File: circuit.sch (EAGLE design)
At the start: 8 parts

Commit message: merged display code into main code, added sch
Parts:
- added IC1: 74HC595N, 74xx-eu:74HC595N
- added R2, R3: 330, HyTechDevices:RESISTORPTH-1/4W
- added R4: 1k, HyTechDevices:RESISTORPTH-1/4W
- added S2: (no value), switch-omron:40-XX
- added U$6: DUAL_7SEG_DISPLAY, HyTechDevices:DUAL_7SEG_DISPLAY
- added U$7, U$8: 2N9304, HyTechDevices:2N9304
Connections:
- new net BJT1_CTRL: R2.1, U$7.BASE
- new net BJT2_CTRL: R3.1, U$8.BASE
- new net D28: R2.2, U$1.D28
- new net D29: R3.2, U$1.D29
- new net DIG1_COL: U$6.P$16, U$7.COLLECTOR
- new net DIG2_COL: U$6.P$11, U$8.COLLECTOR
- new net N$1: IC1A.QE, U$6.P$1
- new net N$10: IC1A.QG, U$6.P$13
- new net N$11: IC1A.QH, U$6.P$6
- new net N$12: R4.1, S2.P, U$1.A15
- new net N$3: IC1A.QB, U$6.P$10
- new net N$4: IC1A.QC, U$6.P$9
- new net N$7: IC1A.QD, U$6.P$7
- new net N$8: IC1A.QA, U$6.P$12
- new net N$9: IC1A.QF, U$6.P$18
- new net RCLK: IC1A.RCK, U$1.A19
- new net SER: IC1A.SER, U$1.A17
- new net SRCLK: IC1A.SCK, U$1.A18
- new net SRCLR: IC1A.SCL, U$1.A20
- net +3V3: now also IC1P.VCC, S2.S
- net GND: now also IC1A.G, IC1P.GND, R4.2, U$7.EMITTER, U$8.EMITTER
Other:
- note added: ""unfreeze" button"
- note added: "BMMCC orientation logger - made by Soohyun Kim"
- note added: "adafruit sensor"
- note added: "record button"
- moved on the sheet: R1, S1

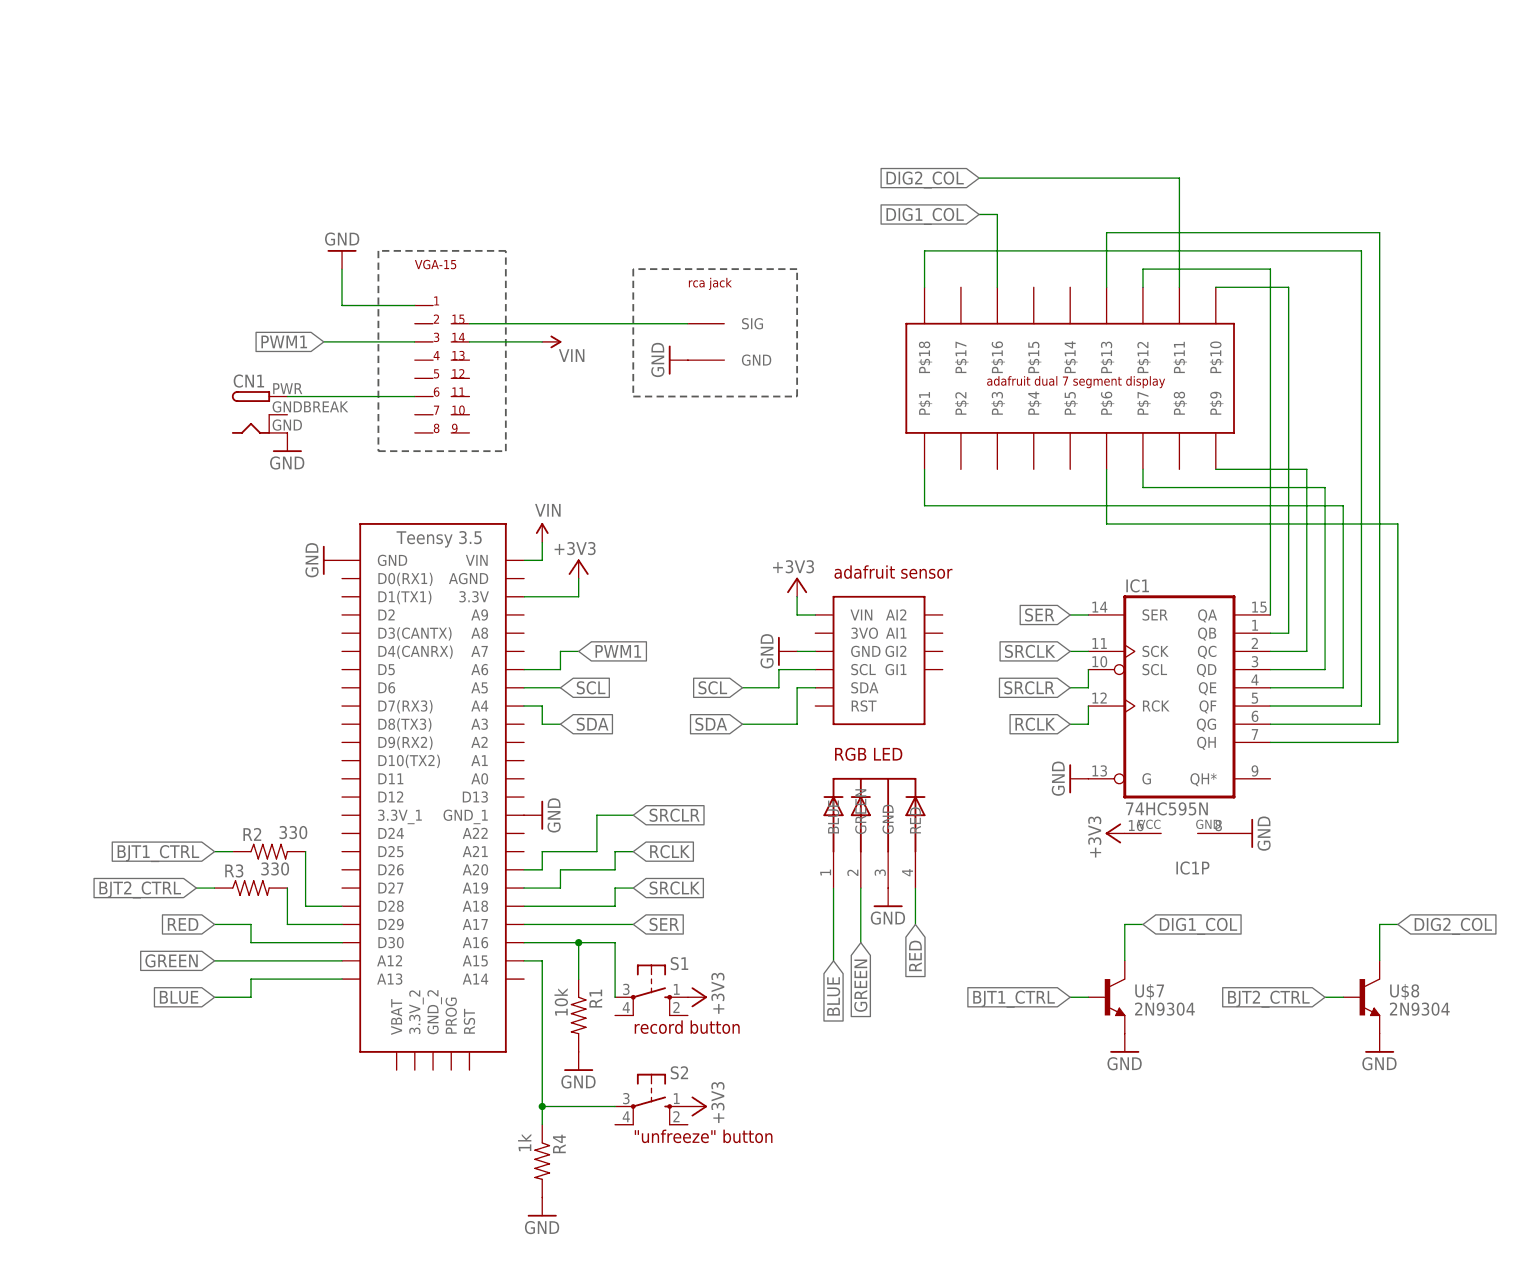
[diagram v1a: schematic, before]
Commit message: added board for main pcb
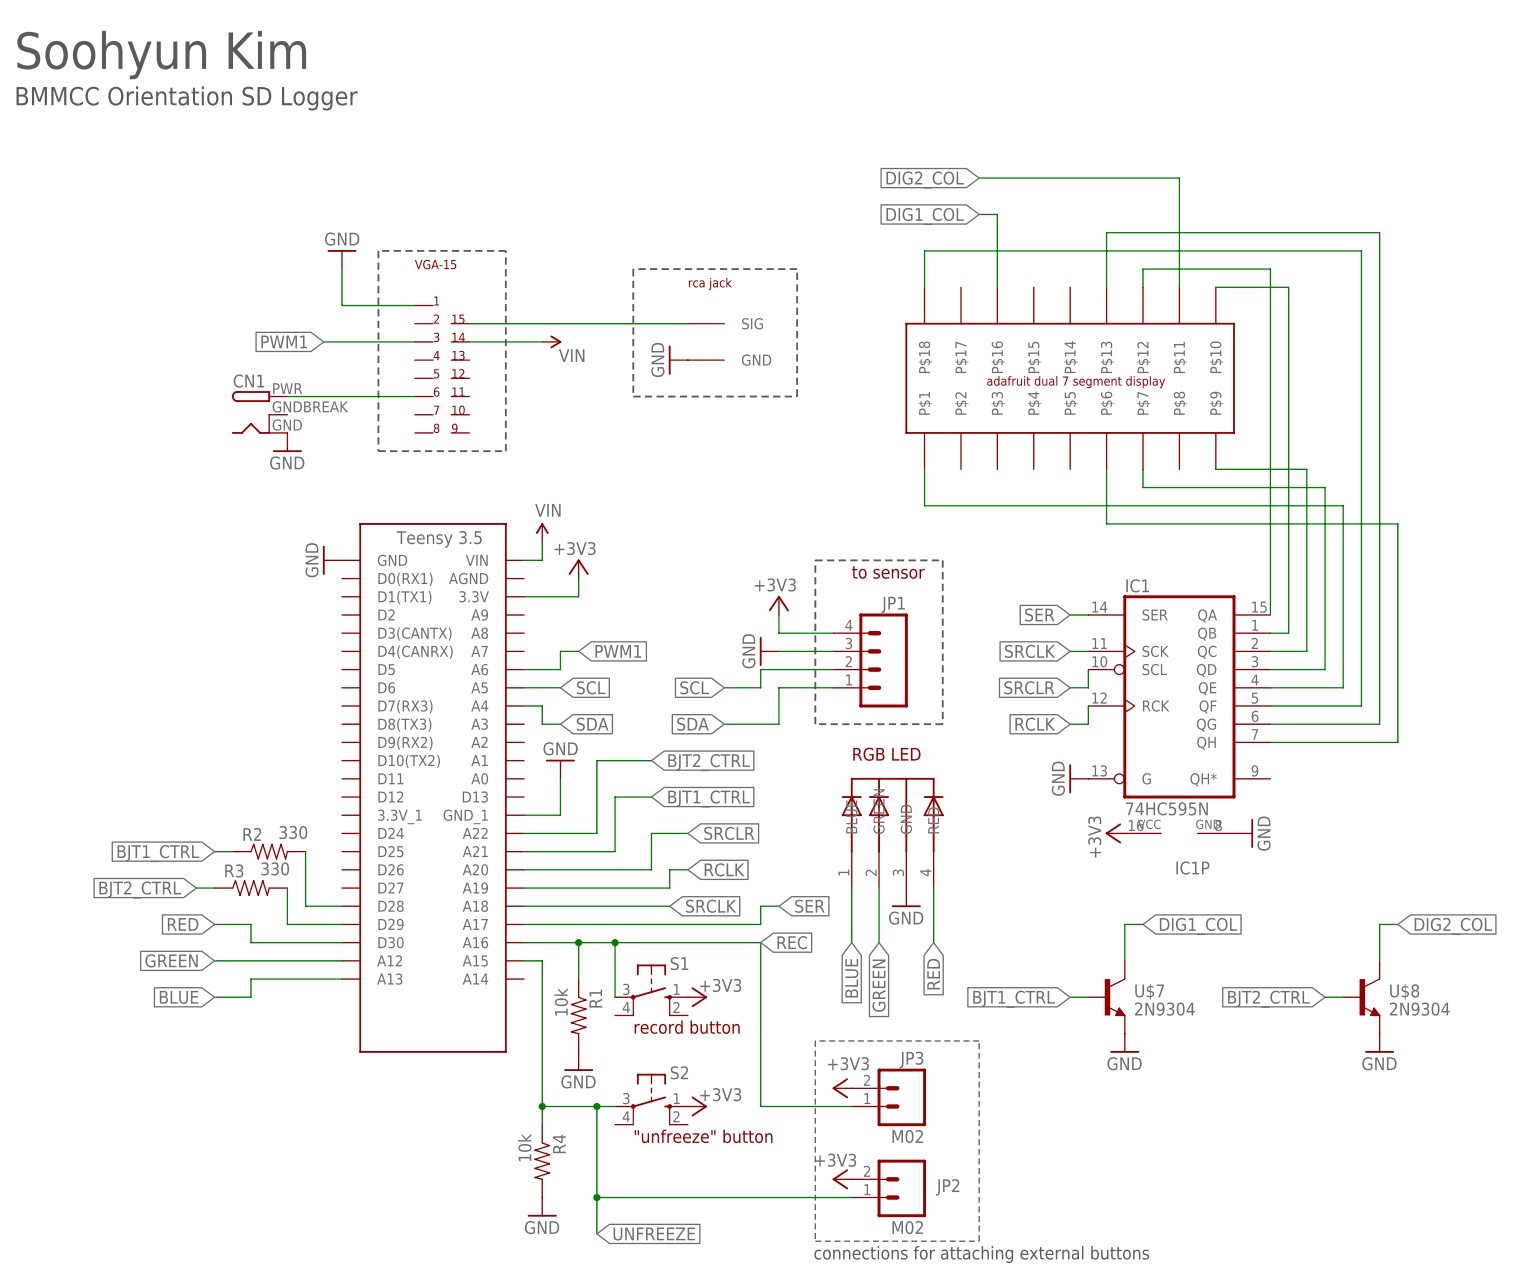
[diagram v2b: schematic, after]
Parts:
- removed U$5: RCA, HyTechDevices:RCA
- added JP1: (no value), HyTechDevices:M04
- added JP2, JP3: M02, HyTechDevices:M02
- R4: value 1k -> 10k
- U$1: value TEENSY_3.5_EXT -> TEENSY_3.5; device HyTechDevices:TEENSY_3.5_EXT -> HyTechDevices:TEENSY_3.5
- U$3: value ADAFRUIT_9DOF -> RCA; device HyTechDevices:ADAFRUIT_9DOF -> HyTechDevices:RCA
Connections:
- removed net N$12: R4.1, S2.P, U$1.A15
- removed net N$2: R1.1, S1.P, U$1.A16
- new net REC: JP3.1, R1.1, S1.P, U$1.A16
- new net UNFREEZE: JP2.1, R4.1, S2.P, U$1.A15
- net +3V3: now also JP1.4, JP2.2, JP3.2; no longer U$3.VIN
- net BJT1_CTRL: now also U$1.A21
- net BJT2_CTRL: now also U$1.A22
- net GND: now also JP1.3; no longer U$5.GND
- net N$5: now also U$3.SIG; no longer U$5.SIG
- net SCL: now also JP1.2; no longer U$3.SCL
- net SDA: now also JP1.1; no longer U$3.SDA
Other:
- note added: "BMMCC Orientation SD Logger"
- note added: "Soohyun Kim"
- note added: "connections for attaching external buttons"
- note added: "to sensor"
- note removed: "BMMCC orientation logger - made by Soohyun Kim"
- note removed: "adafruit sensor"

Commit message: final?
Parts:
- added U$5: SLIDE_SWITCH, HyTechDevices:SLIDE_SWITCH
- U$4: value LED_5MM_RGB -> LED_5MM_RGBSTRAIGHT; device HyTechDevices:LED_5MM_RGB -> HyTechDevices:LED_5MM_RGBSTRAIGHT
- renumbered S1 to S3, S2 to S4
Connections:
- new net N$2: U$2.P$14, U$5.P
- net VIN: now also U$5.S; no longer U$2.P$14
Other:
- note added: "power switch / reset"
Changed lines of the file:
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@@
 <part name="GND5" library="HyTechSymbols" deviceset="GND" device=""/>
 <part name="GND6" library="HyTechSymbols" deviceset="GND" device=""/>
-<part name="S1" library="switch-omron" library_urn="urn:adsk.eagle:library:377" deviceset="40-XX" device="" package3d_urn="urn:adsk.eagle:package:27483/1"/>
 <part name="+3V3" library="supply1" library_urn="urn:adsk.eagle:library:371" deviceset="+3V3" device=""/>
-<part name="U$4" library="HyTechDevices" deviceset="LED_5MM_RGB" device=""/>
 <part name="GND7" library="HyTechSymbols" deviceset="GND" device=""/>
 <part name="GND8" library="HyTechSymbols" deviceset="GND" device=""/>
@@
 <part name="R2" library="HyTechDevices" deviceset="RESISTOR" device="PTH-1/4W" value="330"/>
 <part name="R3" library="HyTechDevices" deviceset="RESISTOR" device="PTH-1/4W" value="330"/>
-<part name="S2" library="switch-omron" library_urn="urn:adsk.eagle:library:377" deviceset="40-XX" device="" package3d_urn="urn:adsk.eagle:package:27483/1"/>
 <part name="+3V5" library="supply1" library_urn="urn:adsk.eagle:library:371" deviceset="+3V3" device=""/>
 <part name="R4" library="HyTechDevices" deviceset="RESISTOR" device="PTH-1/4W" value="10k"/>
@@
 <part name="U$1" library="HyTechDevices" deviceset="TEENSY_3.5" device=""/>
 <part name="U$2" library="HyTechDevices" deviceset="VGA-15" device=""/>
+<part name="U$4" library="HyTechDevices" deviceset="LED_5MM_RGB" device="STRAIGHT"/>
+<part name="U$5" library="HyTechDevices" deviceset="SLIDE_SWITCH" device=""/>
+<part name="S3" library="switch-omron" deviceset="40-XX" device="" package3d_urn="urn:adsk.eagle:package:27483/1"/>
+<part name="S4" library="switch-omron" deviceset="40-XX" device="" package3d_urn="urn:adsk.eagle:package:27483/1"/>
 </parts>
 <sheets>
@@
 <wire x1="106.68" y1="-3.556" x2="106.68" y2="24.384" width="0.1524" layer="97" style="shortdash"/>
 <wire x1="106.68" y1="24.384" x2="83.82" y2="24.384" width="0.1524" layer="97" style="shortdash"/>
+<text x="58.42" y="106.68" size="1.778" layer="94">power switch / reset</text>
 </plain>
 <instances>
@@
 <attribute name="VALUE" x="7.62" y="104.14" size="1.778" layer="96"/>
 </instance>
-<instance part="SUPPLY1" gate="G$1" x="45.72" y="121.92" smashed="yes" rot="R270">
-<attribute name="VALUE" x="51.816" y="120.904" size="1.778" layer="96" rot="R180"/>
+<instance part="SUPPLY1" gate="G$1" x="55.88" y="104.14" smashed="yes" rot="R270">
+<attribute name="VALUE" x="61.976" y="103.124" size="1.778" layer="96" rot="R180"/>
 </instance>
 <instance part="SUPPLY2" gate="G$1" x="45.72" y="93.98" smashed="yes">
@@
 <attribute name="VALUE" x="12.7" y="93.98" size="1.778" layer="96" rot="R270"/>
 </instance>
-<instance part="S1" gate="1" x="60.96" y="30.48" smashed="yes" rot="R270">
-<attribute name="NAME" x="63.5" y="34.29" size="1.778" layer="95"/>
-<attribute name="VALUE" x="64.135" y="34.29" size="1.778" layer="96"/>
-</instance>
 <instance part="+3V3" gate="G$1" x="68.58" y="30.48" smashed="yes" rot="R270">
 <attribute name="VALUE" x="73.66" y="33.02" size="1.778" layer="96" rot="R180"/>
 </instance>
-<instance part="U$4" gate="G$1" x="96.52" y="60.96" smashed="yes"/>
 <instance part="GND7" gate="1" x="96.52" y="43.18" smashed="yes">
 <attribute name="VALUE" x="93.98" y="40.64" size="1.778" layer="96"/>
@@
 <attribute name="VALUE" x="6.35" y="47.498" size="1.778" layer="96"/>
 </instance>
-<instance part="S2" gate="1" x="60.96" y="15.24" smashed="yes" rot="R270">
-<attribute name="NAME" x="63.5" y="19.05" size="1.778" layer="95"/>
-<attribute name="VALUE" x="64.135" y="19.05" size="1.778" layer="96"/>
-</instance>
 <instance part="+3V5" gate="G$1" x="68.58" y="15.24" smashed="yes" rot="R270">
 <attribute name="VALUE" x="73.66" y="17.78" size="1.778" layer="96" rot="R180"/>
@@
 <instance part="U$1" gate="G$1" x="20.32" y="22.86" smashed="yes"/>
 <instance part="U$2" gate="G$1" x="27.94" y="127" smashed="yes"/>
+<instance part="U$4" gate="G$1" x="96.52" y="60.96" smashed="yes"/>
+<instance part="U$5" gate="G$1" x="50.8" y="109.22" smashed="yes" rot="R270"/>
+<instance part="S3" gate="1" x="60.96" y="30.48" smashed="yes" rot="R270">
+<attribute name="VALUE" x="64.135" y="34.29" size="1.778" layer="96"/>
+</instance>
+<instance part="S4" gate="1" x="60.96" y="15.24" smashed="yes" rot="R270">
+<attribute name="VALUE" x="64.135" y="19.05" size="1.778" layer="96"/>
+</instance>
 </instances>
 <busses>
@@
 </segment>
 <segment>
-<pinref part="U$4" gate="G$1" pin="GND"/>
-<pinref part="GND7" gate="1" pin="GND"/>
-</segment>
-<segment>
 <pinref part="IC1" gate="P" pin="GND"/>
 <pinref part="GND9" gate="1" pin="GND"/>
@@
 <pinref part="U$1" gate="G$1" pin="GND"/>
 </segment>
+<segment>
+<pinref part="GND7" gate="1" pin="GND"/>
+<pinref part="U$4" gate="G$1" pin="GND"/>
+</segment>
 </net>
 <net name="VIN" class="0">
@@
 </segment>
 <segment>
-<wire x1="45.72" y1="121.92" x2="35.56" y2="121.92" width="0.1524" layer="91"/>
+<pinref part="U$5" gate="G$1" pin="S"/>
 <pinref part="SUPPLY1" gate="G$1" pin="VIN"/>
-<pinref part="U$2" gate="G$1" pin="P$14"/>
 </segment>
 </net>
@@
 </segment>
 <segment>
-<pinref part="S1" gate="1" pin="S"/>
-<pinref part="+3V3" gate="G$1" pin="+3V3"/>
-</segment>
-<segment>
 <pinref part="IC1" gate="P" pin="VCC"/>
 <pinref part="+3V4" gate="G$1" pin="+3V3"/>
 </segment>
 <segment>
-<pinref part="S2" gate="1" pin="S"/>
-<pinref part="+3V5" gate="G$1" pin="+3V3"/>
-</segment>
-<segment>
 <pinref part="JP2" gate="G$1" pin="2"/>
 <pinref part="+3V6" gate="G$1" pin="+3V3"/>
@@
 <pinref part="JP3" gate="G$1" pin="2"/>
 <pinref part="+3V7" gate="G$1" pin="+3V3"/>
+</segment>
+<segment>
+<pinref part="+3V3" gate="G$1" pin="+3V3"/>
+<pinref part="S3" gate="1" pin="S"/>
+</segment>
+<segment>
+<pinref part="+3V5" gate="G$1" pin="+3V3"/>
+<pinref part="S4" gate="1" pin="S"/>
 </segment>
 </net>
@@
 <net name="RED" class="0">
 <segment>
-<pinref part="U$4" gate="G$1" pin="RED"/>
 <wire x1="100.33" y1="45.72" x2="100.33" y2="38.1" width="0.1524" layer="91"/>
 <label x="100.33" y="38.1" size="1.778" layer="95" rot="R270" xref="yes"/>
+<pinref part="U$4" gate="G$1" pin="RED"/>
 </segment>
 <segment>
@@
 <net name="GREEN" class="0">
 <segment>
-<pinref part="U$4" gate="G$1" pin="GREEN"/>
 <wire x1="92.71" y1="45.72" x2="92.71" y2="38.1" width="0.1524" layer="91"/>
 <label x="92.71" y="38.1" size="1.778" layer="95" rot="R270" xref="yes"/>
+<pinref part="U$4" gate="G$1" pin="GREEN"/>
 </segment>
 <segment>
@@
 <net name="BLUE" class="0">
 <segment>
-<pinref part="U$4" gate="G$1" pin="BLUE"/>
 <wire x1="88.9" y1="45.72" x2="88.9" y2="38.1" width="0.1524" layer="91"/>
 <label x="88.9" y="38.1" size="1.778" layer="95" rot="R270" xref="yes"/>
+<pinref part="U$4" gate="G$1" pin="BLUE"/>
 </segment>
 <segment>
@@
 <net name="REC" class="0">
 <segment>
-<pinref part="S1" gate="1" pin="P"/>
 <wire x1="55.88" y1="38.1" x2="55.88" y2="30.48" width="0.1524" layer="91"/>
 <wire x1="43.18" y1="38.1" x2="50.8" y2="38.1" width="0.1524" layer="91"/>
@@
 <label x="76.2" y="38.1" size="1.778" layer="95" xref="yes"/>
 <pinref part="U$1" gate="G$1" pin="A16"/>
+<pinref part="S3" gate="1" pin="P"/>
 </segment>
 </net>
@@
 <wire x1="45.72" y1="35.56" x2="45.72" y2="15.24" width="0.1524" layer="91"/>
 <wire x1="45.72" y1="15.24" x2="53.34" y2="15.24" width="0.1524" layer="91"/>
-<pinref part="S2" gate="1" pin="P"/>
 <wire x1="53.34" y1="15.24" x2="55.88" y2="15.24" width="0.1524" layer="91"/>
 <wire x1="45.72" y1="15.24" x2="45.72" y2="12.7" width="0.1524" layer="91"/>
@@
 <junction x="53.34" y="2.54"/>
 <pinref part="U$1" gate="G$1" pin="A15"/>
-</segment>
-</net>
+<pinref part="S4" gate="1" pin="P"/>
+</segment>
+</net>
+<net name="N$2" class="0">
+<segment>
+<pinref part="U$2" gate="G$1" pin="P$14"/>
+<wire x1="35.56" y1="121.92" x2="43.18" y2="121.92" width="0.1524" layer="91"/>
+<wire x1="43.18" y1="121.92" x2="43.18" y2="106.68" width="0.1524" layer="91"/>
+<pinref part="U$5" gate="G$1" pin="P"/>
+<wire x1="43.18" y1="106.68" x2="45.72" y2="106.68" width="0.1524" layer="91"/>
+</segment>
+</net>

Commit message: final
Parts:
- U$4: value LED_5MM_RGBSTRAIGHT -> LED_5MM_RGB; device HyTechDevices:LED_5MM_RGBSTRAIGHT -> HyTechDevices:LED_5MM_RGB
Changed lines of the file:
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@@
 <part name="U$1" library="HyTechDevices" deviceset="TEENSY_3.5" device=""/>
 <part name="U$2" library="HyTechDevices" deviceset="VGA-15" device=""/>
-<part name="U$4" library="HyTechDevices" deviceset="LED_5MM_RGB" device="STRAIGHT"/>
 <part name="U$5" library="HyTechDevices" deviceset="SLIDE_SWITCH" device=""/>
 <part name="S3" library="switch-omron" deviceset="40-XX" device="" package3d_urn="urn:adsk.eagle:package:27483/1"/>
 <part name="S4" library="switch-omron" deviceset="40-XX" device="" package3d_urn="urn:adsk.eagle:package:27483/1"/>
+<part name="U$4" library="HyTechDevices" deviceset="LED_5MM_RGB" device=""/>
 </parts>
 <sheets>
@@
 <instance part="U$1" gate="G$1" x="20.32" y="22.86" smashed="yes"/>
 <instance part="U$2" gate="G$1" x="27.94" y="127" smashed="yes"/>
-<instance part="U$4" gate="G$1" x="96.52" y="60.96" smashed="yes"/>
 <instance part="U$5" gate="G$1" x="50.8" y="109.22" smashed="yes" rot="R270"/>
 <instance part="S3" gate="1" x="60.96" y="30.48" smashed="yes" rot="R270">
@@
 <attribute name="VALUE" x="64.135" y="19.05" size="1.778" layer="96"/>
 </instance>
+<instance part="U$4" gate="G$1" x="96.52" y="60.96" smashed="yes"/>
 </instances>
 <busses>
